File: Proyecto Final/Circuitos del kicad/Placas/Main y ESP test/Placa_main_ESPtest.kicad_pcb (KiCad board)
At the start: 2 copper layers, 135.7 x 98.3 mm, 21 parts, among them J1 12v, J2 Conn_02x05_Odd_Even, J3 Conn_02x06_Odd_Even, J4 Conn_01x08, J5 Conn_01x08, J6 Conn_01x06, U1 LM7805, U2 ESP-12E, U3 ATmega328P-P, U4 LM1117-3.3, U5 BOB-12009, Y1 16MHz

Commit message: a
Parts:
- moved U2 15.8 mm to (70.4, 59.3)
- moved J6 15.8 mm to (54.2, 65.5)
- moved J4 15.8 mm to (75.6, 47.9)
- moved J5 15.8 mm to (75.5, 70.5)
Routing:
- net +5V: track 221.9 -> 241.1 mm, vias 0 -> 3
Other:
- board size 135.7 x 98.3 mm -> 119.9 x 98.9 mm
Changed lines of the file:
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@@
   )
   (footprint "Connector_PinHeader_2.54mm:PinHeader_1x08_P2.54mm_Vertical" (layer "F.Cu")
-    (at 59.805 48.54 -90)
+    (at 75.553 47.892 -90)
     (descr "Through hole straight pin header, 1x08, 2.54mm pitch, single row")
     (tags "Through hole pin header THT 1x08 2.54mm single row")
@@
   )
   (footprint "Connector_PinHeader_2.54mm:PinHeader_1x06_P2.54mm_Vertical" (layer "F.Cu")
-    (at 38.41 66.1 180)
+    (at 54.158 65.452 180)
     (descr "Through hole straight pin header, 1x06, 2.54mm pitch, single row")
     (tags "Through hole pin header THT 1x06 2.54mm single row")
@@
   )
   (footprint "Connector_PinHeader_2.54mm:PinHeader_1x08_P2.54mm_Vertical" (layer "F.Cu")
-    (at 59.775 71.16 -90)
+    (at 75.523 70.512 -90)
     (descr "Through hole straight pin header, 1x08, 2.54mm pitch, single row")
     (tags "Through hole pin header THT 1x08 2.54mm single row")
@@
   )
   (footprint "RF_Module:ESP-12E" (layer "F.Cu")
-    (at 54.69 59.99 -90)
+    (at 70.438 59.342 -90)
     (descr "Wi-Fi Module, http://wiki.ai-thinker.com/_media/esp8266/docs/aithinker_esp_12f_datasheet_en.pdf")
     (tags "Wi-Fi Module")
@@
   (gr_line (start 129.82 128.705) (end 129.81 110.695) (layer "Dwgs.User") (width 0.15))
   (gr_line (start 129.81 110.695) (end 127.77 110.695) (layer "Dwgs.User") (width 0.15))
-  (gr_rect (start 67.31 46.365) (end 34.65 73.295) (layer "Edge.Cuts") (width 0.2) (fill none))
+  (gr_rect (start 83.058 45.717) (end 50.398 72.647) (layer "Edge.Cuts") (width 0.2) (fill none))
   (gr_rect (start 170.3355 53.43) (end 94.67 144.65) (layer "Edge.Cuts") (width 0.2) (fill none))
   (via (at 97.25 133.82) (size 4) (drill 3.5) (layers "F.Cu" "B.Cu") (free) (net 0))
@@
   (via (at 121.28 73.68) (size 2) (drill 0.75) (layers "F.Cu" "B.Cu") (free) (net 0))
   (segment (start 136.251202 110.618894) (end 136.398 110.765692) (width 1) (layer "F.Cu") (net 1))
-  (segment (start 44.19 67.59) (end 44.19 68.965) (width 1) (layer "F.Cu") (net 1))
+  (segment (start 59.938 66.942) (end 59.938 68.317) (width 1) (layer "F.Cu") (net 1))
   (segment (start 107.4575 81.1775) (end 107.455 81.18) (width 1) (layer "F.Cu") (net 1))
-  (segment (start 44.19 68.965) (end 41.9975 71.1575) (width 1) (layer "F.Cu") (net 1))
+  (segment (start 59.938 68.317) (end 57.7455 70.5095) (width 1) (layer "F.Cu") (net 1))
   (segment (start 136.398 113.284) (end 138.43 115.316) (width 1) (layer "F.Cu") (net 1))
   (segment (start 116.3525 88.44) (end 116.3525 91.94) (width 0.8) (layer "F.Cu") (net 1))
@@
   (segment (start 138.41 129.55) (end 138.45 129.51) (width 1) (layer "B.Cu") (net 1))
   (segment (start 140.056 65.518) (end 140.056 64.414) (width 1) (layer "B.Cu") (net 1))
+  (segment (start 114.3 66.04) (end 114.3 61.976) (width 1) (layer "F.Cu") (net 2))
+  (via (at 114.3 61.976) (size 2) (drill 0.75) (layers "F.Cu" "B.Cu") (net 2))
+  (via (at 107.48546 58.565462) (size 2) (drill 0.75) (layers "F.Cu" "B.Cu") (free) (net 2))
+  (via (at 114.3 66.04) (size 2) (drill 0.75) (layers "F.Cu" "B.Cu") (net 2))
   (segment (start 138.1 100.38) (end 138.1 97.43) (width 1.2) (layer "B.Cu") (net 2))
   (segment (start 154.686 67.818) (end 156.464 69.596) (width 1.2) (layer "B.Cu") (net 2))
@@
   (segment (start 143.482 74.45) (end 145.796 72.136) (width 1.2) (layer "B.Cu") (net 2))
   (segment (start 142.0275 97.26) (end 142.86 97.26) (width 1) (layer "B.Cu") (net 2))
+  (segment (start 113.83 66.51) (end 114.3 66.04) (width 1) (layer "B.Cu") (net 2))
   (segment (start 142.7725 74.3) (end 142.6225 74.45) (width 0.8) (layer "B.Cu") (net 2))
   (segment (start 112.99 114.26) (end 135.77 114.26) (width 1.2) (layer "B.Cu") (net 2))
@@
   (segment (start 130.976988 72.985012) (end 132.207024 72.985012) (width 1.2) (layer "B.Cu") (net 2))
   (segment (start 147.574 67.818) (end 154.686 67.818) (width 1.2) (layer "B.Cu") (net 2))
+  (segment (start 114.3 58.166) (end 113.03 56.896) (width 1) (layer "B.Cu") (net 2))
   (segment (start 138.11 111.96) (end 138.11 99.3695) (width 1.2) (layer "B.Cu") (net 2))
   (segment (start 139.192 72.898) (end 142.36 72.898) (width 1.2) (layer "B.Cu") (net 2))
@@
   (segment (start 154.0475 75.194) (end 154.676 75.194) (width 1.2) (layer "B.Cu") (net 2))
   (segment (start 135.8 114.27) (end 138.11 111.96) (width 1.2) (layer "B.Cu") (net 2))
+  (segment (start 114.3 61.976) (end 114.3 58.166) (width 1) (layer "B.Cu") (net 2))
   (segment (start 126.492 77.47) (end 130.976988 72.985012) (width 1.2) (layer "B.Cu") (net 2))
   (segment (start 142.86 97.26) (end 143.68 98.08) (width 1) (layer "B.Cu") (net 2))
@@
   (segment (start 111.14 66.51) (end 103.8225 66.51) (width 1.2) (layer "B.Cu") (net 2))
   (segment (start 145.796 69.596) (end 147.574 67.818) (width 1.2) (layer "B.Cu") (net 2))
+  (segment (start 109.154922 56.896) (end 107.48546 58.565462) (width 1) (layer "B.Cu") (net 2))
   (segment (start 106.4 103.68) (end 108.94 103.68) (width 1.2) (layer "B.Cu") (net 2))
   (segment (start 140.49 72.51) (end 142.748 72.51) (width 0.25) (layer "B.Cu") (net 2))
   (segment (start 140.056 70.118) (end 140.056 72.898) (width 1) (layer "B.Cu") (net 2))
+  (segment (start 113.03 56.896) (end 109.154922 56.896) (width 1) (layer "B.Cu") (net 2))
   (segment (start 134.4075 92.18) (end 137.87 92.18) (width 1.2) (layer "B.Cu") (net 2))
   (segment (start 138.27 97.26) (end 138.1 97.43) (width 1) (layer "B.Cu") (net 2))
@@
   (segment (start 135.8 114.27) (end 136.19 114.66) (width 1) (layer "B.Cu") (net 2))
   (segment (start 106.4 103.68) (end 106.4425 103.7225) (width 0.8) (layer "B.Cu") (net 2))
+  (segment (start 111.14 66.51) (end 113.83 66.51) (width 1) (layer "B.Cu") (net 2))
   (segment (start 100.838 76.454) (end 101.854 77.47) (width 1.2) (layer "B.Cu") (net 2))
   (segment (start 142.36 72.898) (end 142.748 72.51) (width 1.2) (layer "B.Cu") (net 2))
@@
   (segment (start 138.248 68) (end 140.15 68) (width 1) (layer "B.Cu") (net 12))
   (segment (start 119.8625 75.0975) (end 119.8625 81.2545) (width 0.8) (layer "F.Cu") (net 13))
-  (segment (start 56.19 69.06) (end 57.235 70.105) (width 1) (layer "F.Cu") (net 13))
-  (segment (start 56.19 67.59) (end 56.19 69.06) (width 1) (layer "F.Cu") (net 13))
-  (segment (start 57.235 70.105) (end 57.235 71.16) (width 1) (layer "F.Cu") (net 13))
+  (segment (start 71.938 68.412) (end 72.983 69.457) (width 1) (layer "F.Cu") (net 13))
+  (segment (start 71.938 66.942) (end 71.938 68.412) (width 1) (layer "F.Cu") (net 13))
+  (segment (start 72.983 69.457) (end 72.983 70.512) (width 1) (layer "F.Cu") (net 13))
   (segment (start 121.28 73.68) (end 119.8625 75.0975) (width 0.8) (layer "F.Cu") (net 13))
   (segment (start 119.8625 81.2545) (end 119.888 81.28) (width 0.8) (layer "F.Cu") (net 13))
@@
   (segment (start 119.888 81.28) (end 119.97975 81.18825) (width 1) (layer "B.Cu") (net 13))
   (segment (start 121.28 73.68) (end 121.3 73.66) (width 0.8) (layer "B.Cu") (net 13))
-  (segment (start 42.025 50.225) (end 44.19 52.39) (width 1) (layer "F.Cu") (net 14))
-  (segment (start 42.025 48.54) (end 42.025 50.225) (width 1) (layer "F.Cu") (net 14))
+  (segment (start 57.773 49.577) (end 59.938 51.742) (width 1) (layer "F.Cu") (net 14))
+  (segment (start 57.773 47.892) (end 57.773 49.577) (width 1) (layer "F.Cu") (net 14))
   (segment (start 109.7025 75.0975) (end 109.7025 81.2545) (width 0.8) (layer "F.Cu") (net 15))
   (segment (start 111.15 73.65) (end 109.7025 75.0975) (width 0.8) (layer "F.Cu") (net 15))
@@
   (segment (start 111.15 73.65) (end 111.14 73.64) (width 0.8) (layer "B.Cu") (net 15))
   (segment (start 111.14 73.64) (end 111.14 71.59) (width 0.8) (layer "B.Cu") (net 15))
-  (segment (start 58.19 68.27) (end 58.19 67.59) (width 1) (layer "F.Cu") (net 22))
-  (segment (start 59.775 71.16) (end 59.775 69.855) (width 1) (layer "F.Cu") (net 22))
-  (segment (start 59.775 69.855) (end 58.19 68.27) (width 1) (layer "F.Cu") (net 22))
+  (segment (start 73.938 67.622) (end 73.938 66.942) (width 1) (layer "F.Cu") (net 22))
+  (segment (start 75.523 70.512) (end 75.523 69.207) (width 1) (layer "F.Cu") (net 22))
+  (segment (start 75.523 69.207) (end 73.938 67.622) (width 1) (layer "F.Cu") (net 22))
   (via (at 125.23325 81.18825) (size 2) (drill 0.75) (layers "F.Cu" "B.Cu") (free) (net 22))
   (segment (start 133.50875 79.48) (end 134.4075 79.48) (width 1) (layer "B.Cu") (net 22))

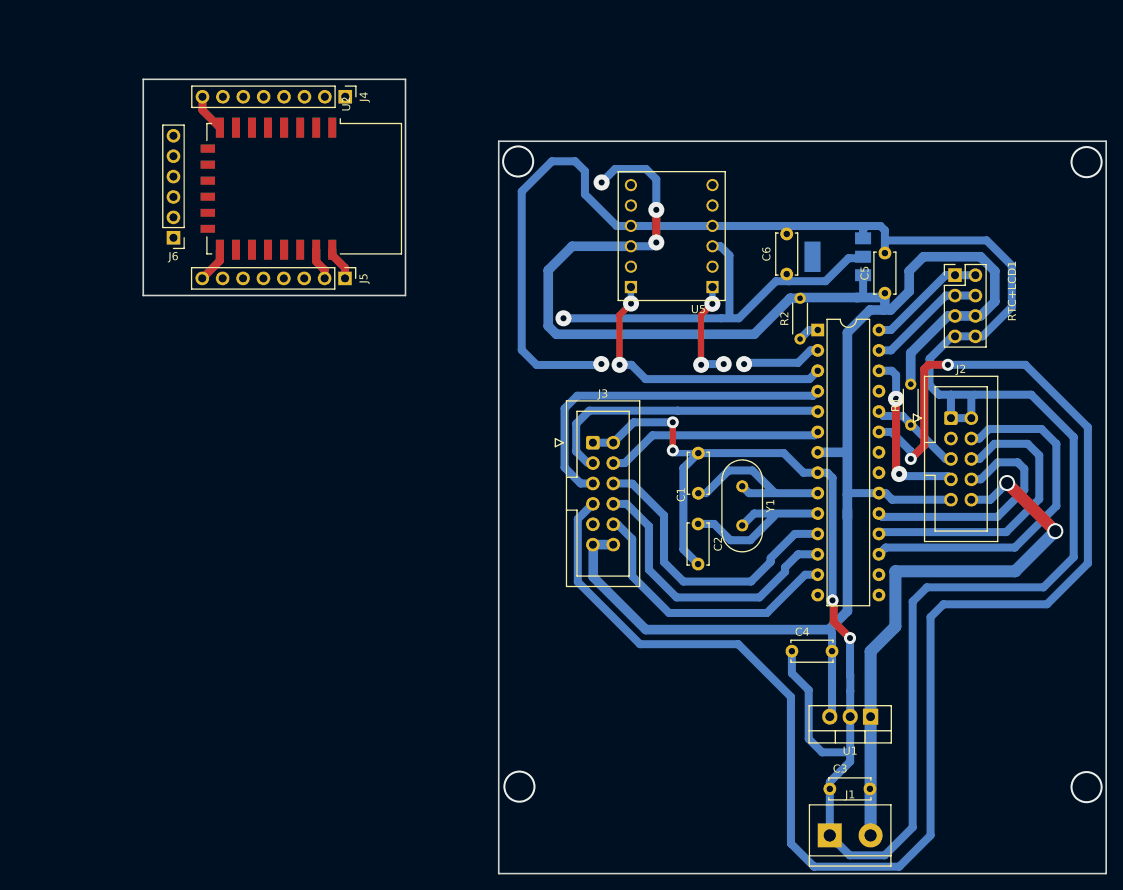
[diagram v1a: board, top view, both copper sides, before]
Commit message: Cambios ancho de agujeros placa main
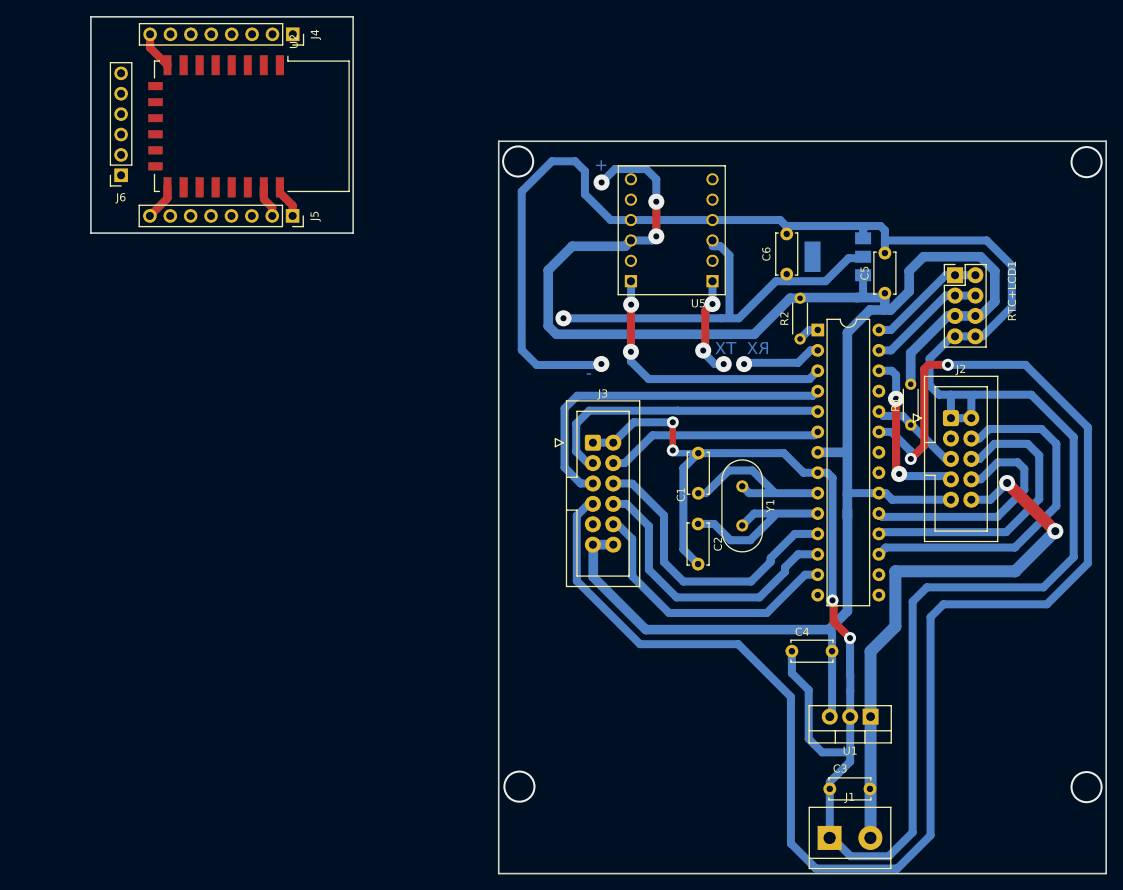
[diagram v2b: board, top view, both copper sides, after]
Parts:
- J4, J5: footprint Connector_PinHeader_2.54mm:PinHeader_1x08_P2.54mm_Vertical -> Connector_PinSocket_2.54mm:PinSocket_1x08_P2.54mm_Vertical
- J6: footprint Connector_PinHeader_2.54mm:PinHeader_1x06_P2.54mm_Vertical -> Connector_PinSocket_2.54mm:PinSocket_1x06_P2.54mm_Vertical
- U5: footprint Conversor_logico_nivel:CONV_BOB-12009 -> Conversor_logico_nivel-2:CONV_BOB-12009
- moved J4 10.2 mm to (69.0, 40.1)
- moved J5 10.2 mm to (69.0, 62.7)
- moved J6 10.2 mm to (47.6, 57.7)
- moved U2 10.2 mm to (63.9, 51.6)
- moved U5 0.72 mm to (116.2, 64.5)
- moved J1 0.31 mm to (135.9, 140.2)
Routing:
- net Net-(U3-Pad3): track 36.2 -> 34.6 mm, vias 0 -> 2
- net Net-(J5-Pad2): track 17.6 -> 16.5 mm, vias 1 -> 3
- net GND: track 353.8 -> 354.4 mm
- net Net-(J3-Pad7): track 189.7 -> 190.3 mm
- net (no net): vias 8 -> 4
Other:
- board size 119.9 x 98.9 mm -> 126.5 x 106.7 mm
- board text added: "+"
- board text added: "-"
- board text added: "RX"
- board text added: "TX"

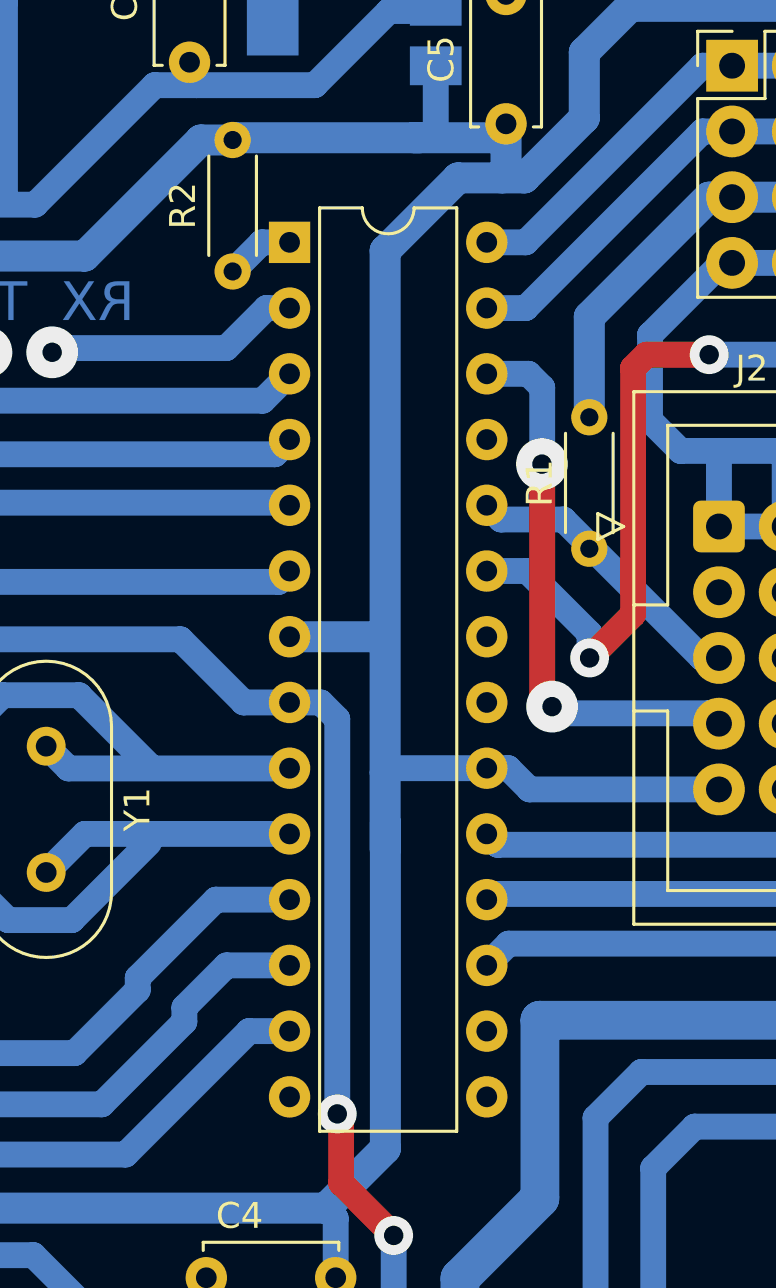
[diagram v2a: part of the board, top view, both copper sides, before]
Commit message: Agregado placa con zocalo piola
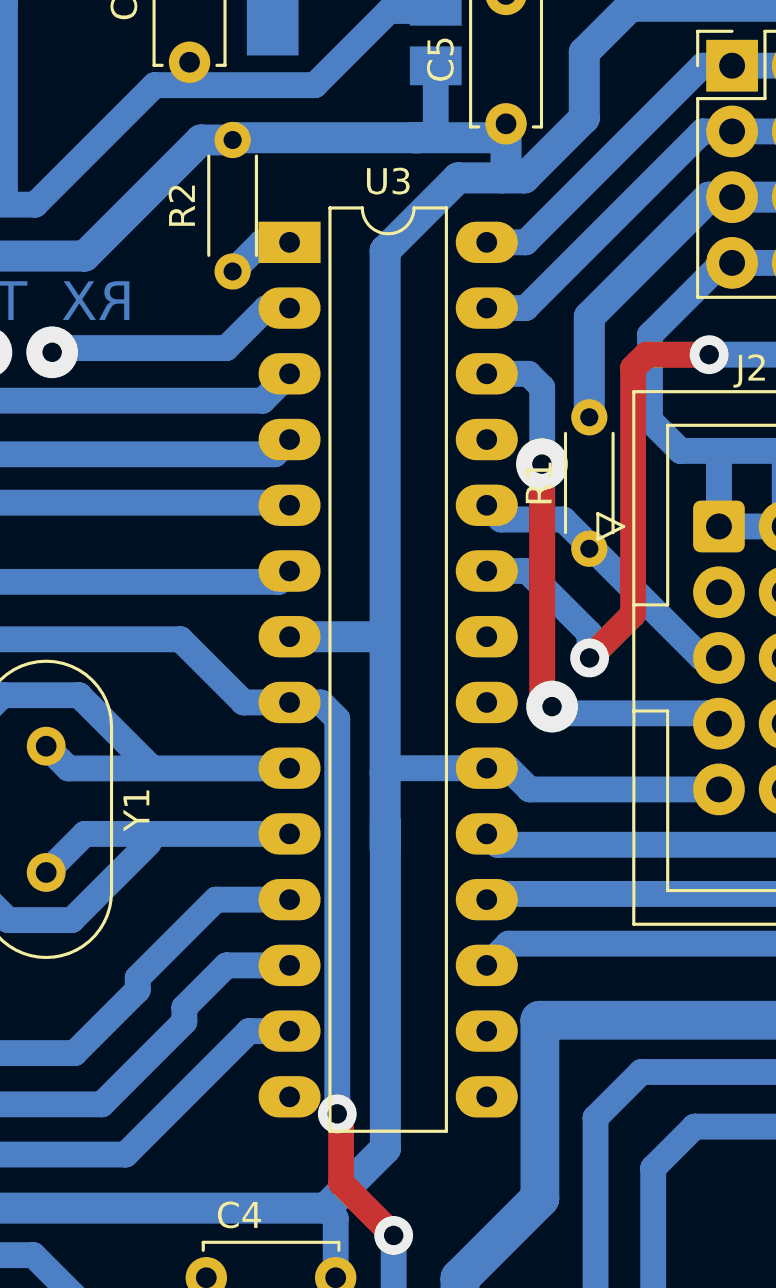
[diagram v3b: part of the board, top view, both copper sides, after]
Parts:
- U3: footprint Package_DIP:DIP-28_W7.62mm -> Package_DIP:DIP-28_W7.62mm_LongPads
